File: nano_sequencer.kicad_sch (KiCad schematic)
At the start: 3 parts, among them U101 74LS125

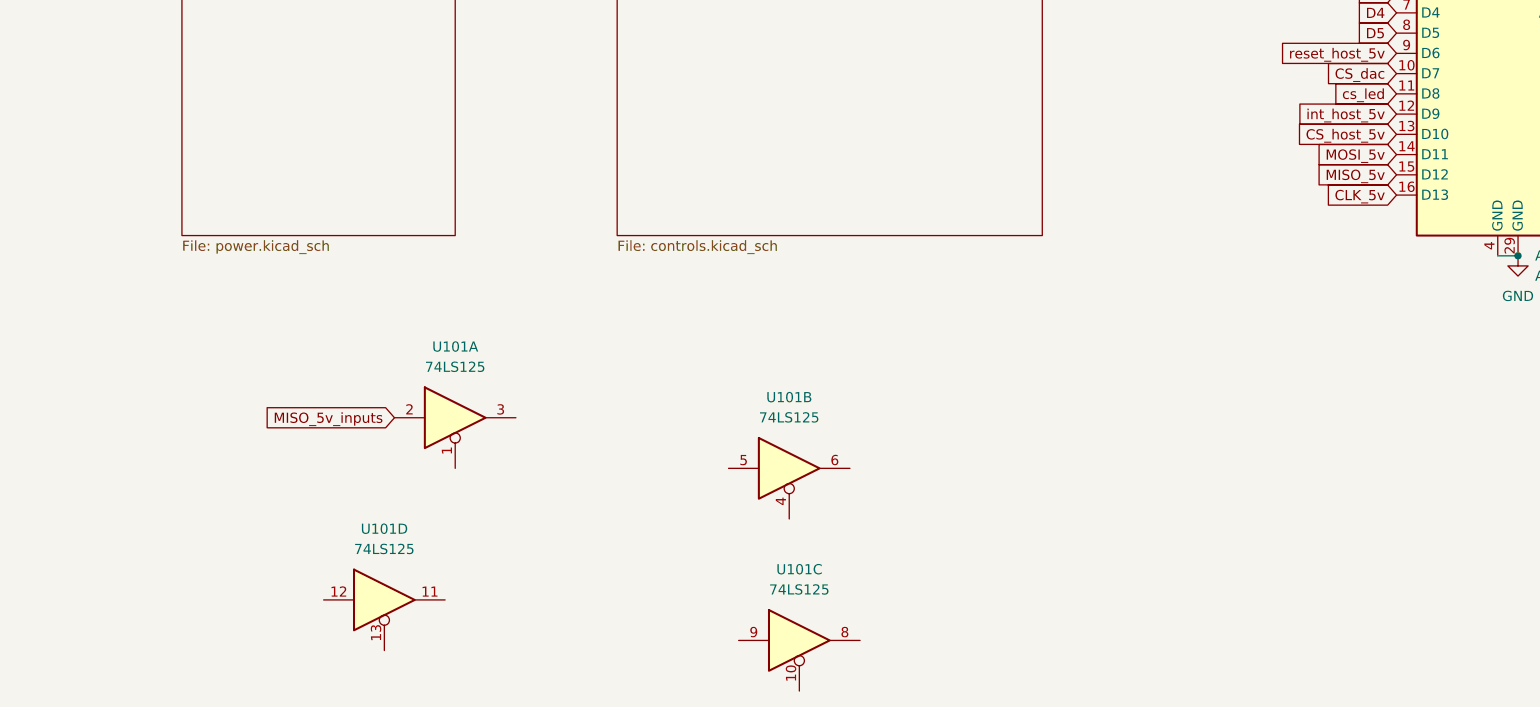
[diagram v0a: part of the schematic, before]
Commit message: schematic done, routed dac ladder
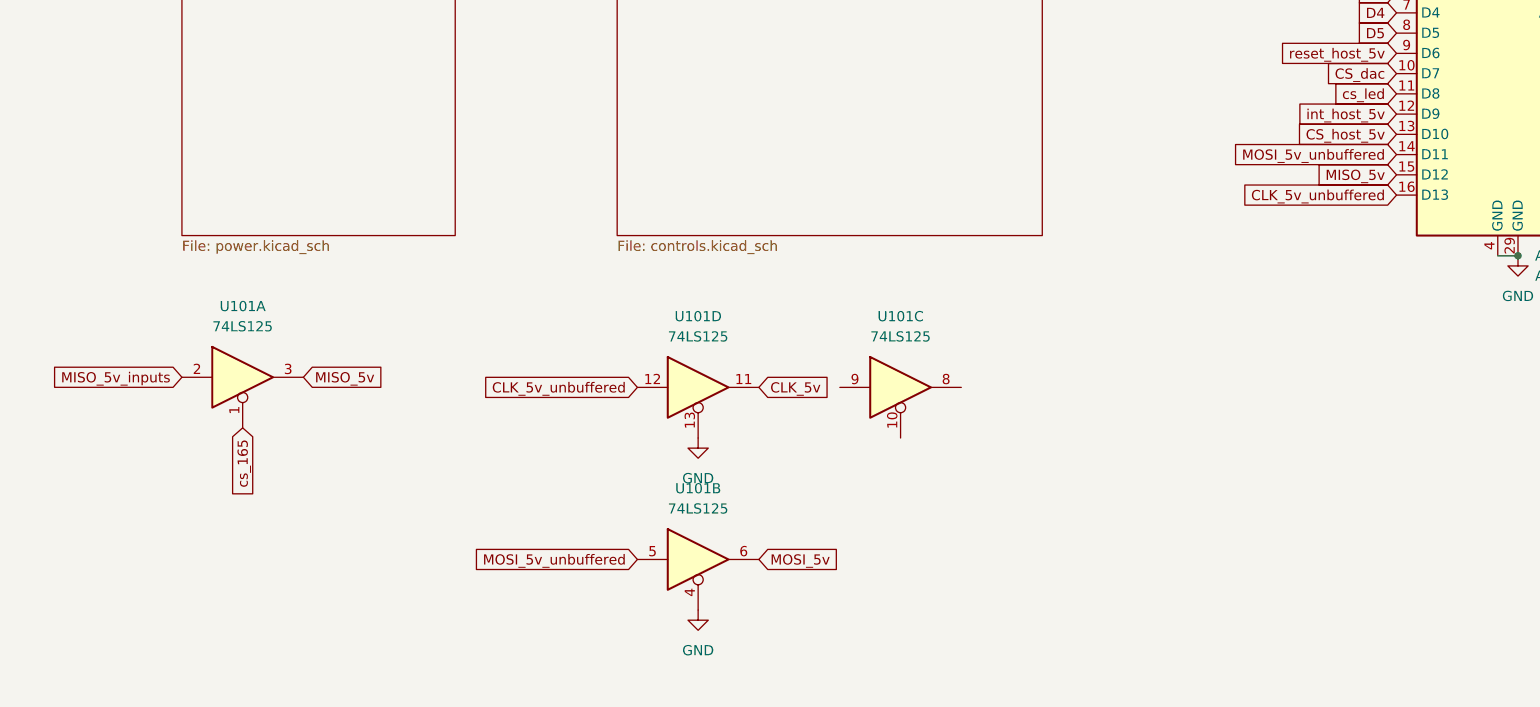
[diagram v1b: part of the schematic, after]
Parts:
- U101: footprint (none) -> Package_SO:SO-14_3.9x8.65mm_P1.27mm
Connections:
- net CLK_5v: now also U101.11; no longer A101.16 (D13)
- net GND: now also U101.13, U101.4
- net MISO_5v: now also U101.3
- net MOSI_5v: now also U101.6; no longer A101.14 (D11)
- net MOSI_5v_unbuffered: now reaches U101.5
- net MOSI_5v_unbuffered: now also A101.14 (D11)
- net CLK_5v_unbuffered: now reaches U101.12
- net CLK_5v_unbuffered: now also A101.16 (D13)
- net cs_165: now reaches U101.1
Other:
- moved on the sheet: U101A, U101B, U101C, U101D

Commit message: added lcsc part numbers and fabrication files
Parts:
- C101: LCSC PN (none) -> C49678
- U101: LCSC PN (none) -> C5598
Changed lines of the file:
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@@
+			)
+		)
+		(property "LCSC PN" ""
+			(at 207.01 118.11 0)
+			(effects
+				(font
+					(size 1.27 1.27)
+				)
 			)
 		)
@@
 			)
 		)
+		(property "LCSC PN" "C5598"
+			(at 106.68 181.61 0)
+			(effects
+				(font
+					(size 1.27 1.27)
+				)
+			)
+		)
 		(pin "14"
 		)
@@
 			)
 		)
+		(property "LCSC PN" "C5598"
+			(at 132.08 160.02 0)
+			(effects
+				(font
+					(size 1.27 1.27)
+				)
+			)
+		)
 		(pin "14"
 		)
@@
 			)
 		)
+		(property "LCSC PN" "C5598"
+			(at 255.27 106.68 0)
+			(effects
+				(font
+					(size 1.27 1.27)
+				)
+			)
+		)
 		(pin "14"
 		)
@@
 			)
 		)
+		(property "LCSC PN" "C5598"
+			(at 106.68 160.02 0)
+			(effects
+				(font
+					(size 1.27 1.27)
+				)
+			)
+		)
 		(pin "14"
 		)
@@
 			)
 		)
+		(property "LCSC PN" "C49678"
+			(at 262.89 93.98 0)
+			(effects
+				(font
+					(size 1.27 1.27)
+				)
+			)
+		)
 		(pin "2"
 		)
@@
 			)
 		)
+		(property "LCSC PN" "C5598"
+			(at 49.53 158.75 0)
+			(effects
+				(font
+					(size 1.27 1.27)
+				)
+			)
+		)
